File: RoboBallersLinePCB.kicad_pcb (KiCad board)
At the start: 2 copper layers, 116 parts, among them J2 Conn_01x04, J3 Conn_02x05_Odd_Even, Q1 SUD08P06-155L, Q2 BSP89, U1 MCP3008, U2 MCP3008, U3 MCP3008, U4 NSL-32, U5 NSL-32, U7 Solenoid-Electric

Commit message: gg
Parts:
- moved R7 97.8 mm to (35.8, 105.7)
- moved D1 83.9 mm to (84.2, 34.1)
- moved D2 83.9 mm to (84.2, 37.5)
- moved D3 83.9 mm to (84.2, 40.8)
- moved D37 83.9 mm to (88.2, 85.7)
- moved D38 83.9 mm to (88.2, 88.7)
- moved D39 83.9 mm to (88.2, 91.8)
- moved D4 83.9 mm to (84.2, 44.2)
- moved D40 83.9 mm to (88.2, 94.8)
- moved D41 83.9 mm to (88.2, 97.9)
- moved D42 83.9 mm to (88.2, 100.9)
- moved D5 83.9 mm to (84.2, 47.6)
- moved D6 83.9 mm to (84.2, 51.0)
- moved J2 83.9 mm to (107.5, 43.0)
- moved Q2 83.9 mm to (110.1, 36.6)
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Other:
- board outline added: 132 x 132 mm

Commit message: PCB + Footprint Revisions
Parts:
- removed J3: Conn_02x05_Odd_Even, Connector_PinHeader_2.54mm:PinHeader_2x05_P2.54mm_Vertical
- added J1: Conn_01x04, Connector_PinHeader_2.54mm:PinHeader_1x04_P2.54mm_Vertical, F.Cu at (331.5, 213.4)
- added U6: NSL-32, Package_DIP:DIP-4_W7.62mm, F.Cu at (326.6, 158.8)
- C1: value 80V 2200uf -> 80v 2200uf
- D1, D10, D11, D12, D13, D14, D15, D16, D17, D18, D19, D2, D20, D21, D22, D23, D24, D3, D4, D5, D6, D7, D8, D9: footprint LED_SMD:LED_1206_3216Metric_Pad1.42x1.75mm_HandSolder -> Capacitor_SMD:C_0805_2012Metric_Pad1.18x1.45mm_HandSolder; moved to B.Cu
- D25, D26, D27, D28, D29, D30, D31, D32, D33, D34, D35, D36, D37, D38, D39, D40, D41, D42, D43, D44, D45, D46, D47, D48: footprint LED_SMD:LED_0805_2012Metric_Pad1.15x1.40mm_HandSolder -> Capacitor_SMD:C_0805_2012Metric_Pad1.18x1.45mm_HandSolder; moved to B.Cu
- D49: value D -> Diode
- J2: value Conn_01x04 -> Bottom PCB; footprint Connector_PinHeader_2.54mm:PinHeader_1x04_P2.54mm_Vertical -> Connector_IDC:IDC-Header_2x05_P2.54mm_Vertical
- Q1: value SUD08P06-155L -> P-Channel; footprint Package_TO_SOT_SMD:TO-252-2 -> Package_TO_SOT_THT:TO-220-3_Vertical
- Q2: value BSP89 -> N-Channel; footprint Package_TO_SOT_SMD:SOT-223-3_TabPin2 -> Package_TO_SOT_THT:TO-220-3_Vertical
- R1, R18: value 750 -> 10k; footprint Resistor_SMD:R_1206_3216Metric_Pad1.30x1.75mm_HandSolder -> Capacitor_SMD:C_0805_2012Metric_Pad1.18x1.45mm_HandSolder
- R10, R11, R12, R13, R14, R15, R16, R17, R19, R2, R20, R21, R22, R23, R24, R3, R4, R5, R6, R8, R9: footprint Resistor_SMD:R_1206_3216Metric_Pad1.30x1.75mm_HandSolder -> Capacitor_SMD:C_0805_2012Metric_Pad1.18x1.45mm_HandSolder; moved to B.Cu
- R25, R26: value 14k -> 750; footprint Resistor_SMD:R_1210_3225Metric_Pad1.30x2.65mm_HandSolder -> Capacitor_SMD:C_0805_2012Metric_Pad1.18x1.45mm_HandSolder; moved to B.Cu
- R27: value 14k -> 10k; footprint Resistor_SMD:R_1210_3225Metric_Pad1.30x2.65mm_HandSolder -> Capacitor_SMD:C_0805_2012Metric_Pad1.18x1.45mm_HandSolder
- R28, R29, R30, R31, R32, R33, R34, R35, R36, R37, R38, R39, R40, R41, R42, R43, R44, R45, R46, R47, R48: footprint Resistor_SMD:R_1210_3225Metric_Pad1.30x2.65mm_HandSolder -> Capacitor_SMD:C_0805_2012Metric_Pad1.18x1.45mm_HandSolder; moved to B.Cu
- R49, R50, R51: value 10K -> 14k; footprint Resistor_THT:R_Axial_DIN0204_L3.6mm_D1.6mm_P7.62mm_Horizontal -> Capacitor_SMD:C_0805_2012Metric_Pad1.18x1.45mm_HandSolder; moved to B.Cu
- R52: value 5K -> 5k; footprint Resistor_SMD:R_0805_2012Metric_Pad1.20x1.40mm_HandSolder -> Capacitor_SMD:C_0805_2012Metric_Pad1.18x1.45mm_HandSolder
- R53: value 19K -> 19k; footprint Resistor_SMD:R_1206_3216Metric_Pad1.30x1.75mm_HandSolder -> Capacitor_SMD:C_0805_2012Metric_Pad1.18x1.45mm_HandSolder
- R54, R55: footprint Resistor_SMD:R_1206_3216Metric_Pad1.30x1.75mm_HandSolder -> Capacitor_SMD:C_0805_2012Metric_Pad1.18x1.45mm_HandSolder
- R56: value 10K -> 10k; footprint Resistor_THT:R_Axial_DIN0204_L3.6mm_D1.6mm_P7.62mm_Horizontal -> Capacitor_SMD:C_0805_2012Metric_Pad1.18x1.45mm_HandSolder
- R7: value 750 -> 165; footprint Resistor_SMD:R_1206_3216Metric_Pad1.30x1.75mm_HandSolder -> Capacitor_SMD:C_0805_2012Metric_Pad1.18x1.45mm_HandSolder; moved to B.Cu
- U1, U2, U3: footprint digikey-footprints:DIP-16_W7.62mm -> Package_DIP:DIP-16_W7.62mm_Socket
- U4: value NSL-32 -> BoostConverter; footprint OptoDevice:Luna_NSL-32 -> BoostConverter:Boost_Convertor_LM2577
- U5: footprint OptoDevice:Luna_NSL-32 -> Package_DIP:DIP-4_W7.62mm
- U7: footprint Connector_PinSocket_2.54mm:PinSocket_1x02_P2.54mm_Vertical -> KickerPad:KickerPad
- moved J2 284.7 mm to (345.4, 199.4)
- moved U7 268.7 mm to (348.8, 170.2)
- moved R1 253.8 mm to (280.2, 193.8)
- moved R18 247.1 mm to (285.0, 202.8)
- moved R53 246.3 mm to (299.4, 181.7)
- moved R54 246.2 mm to (299.4, 184.7)
- moved R55 246.1 mm to (299.4, 187.7)
- moved R27 243.7 mm to (289.8, 187.7)
- moved Q2 240.7 mm to (316.7, 159.9)
- moved U5 235.6 mm to (326.6, 152.1)
- moved C1 230.6 mm to (310.9, 209.5)
- moved R56 230.6 mm to (299.4, 190.7)
- moved D49 229.8 mm to (265.7, 219.7)
- moved R52 227.6 mm to (299.4, 178.7)
- moved Q1 223.1 mm to (316.7, 154.0)
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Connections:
- D25 pad 1: Net-(D25-K) -> CH01
- D26 pad 1: Net-(D26-K) -> CH11
- D27 pad 1: Net-(D27-K) -> CH21
- D28 pad 1: Net-(D28-K) -> CH31
- D29 pad 1: Net-(D29-K) -> CH41
- D30 pad 1: Net-(D30-K) -> CH51
- D31 pad 1: Net-(D31-K) -> CH61
- D32 pad 1: Net-(D32-K) -> CH71
- D33 pad 1: Net-(D33-K) -> CH02
- D34 pad 1: Net-(D34-K) -> CH12
- D35 pad 1: Net-(D35-K) -> CH22
- D36 pad 1: Net-(D36-K) -> CH32
- D37 pad 1: Net-(D37-K) -> CH42
- D38 pad 1: Net-(D38-K) -> CH52
- D39 pad 1: Net-(D39-K) -> CH62
- D40 pad 1: Net-(D40-K) -> CH72
- D41 pad 1: Net-(D41-K) -> CH03
- D42 pad 1: Net-(D42-K) -> CH13
- D43 pad 1: Net-(D43-K) -> CH23
- D44 pad 1: Net-(D44-K) -> CH33
- D45 pad 1: Net-(D45-K) -> CH43
- D46 pad 1: Net-(D46-K) -> CH53
- D47 pad 1: Net-(D47-K) -> CH63
- D48 pad 1: Net-(D48-K) -> CH73
- D49 pad 1: Net-(D49-K) -> Net-(D49-A)
- D49 pad 2: Net-(D49-A) -> Net-(D49-K)
- J2 pad 1: Kicker -> 12v
- J2 pad 2: 3.3V -> CSLS1
- J2 pad 3: GND -> 3.3v
- J2 pad 4: 12V -> CSLS2
- Q1 pad 2: Net-(D49-A) -> Net-(D49-K)
- Q1 pad 3: GND -> 48v
- Q2 pad 2: Net-(D49-K) -> Net-(D49-A)
- Q2 pad 3: 48v -> GND
- R1 pad 1: Net-(D1-A) -> CSLS1
- R1 pad 2: 3.3v -> unconnected-(R1-Pad2)
- R10 pad 1: Net-(D10-A) -> Net-(D9-A)
- R11 pad 1: Net-(D11-A) -> Net-(D10-A)
- R12 pad 1: Net-(D12-A) -> Net-(D11-A)
- R13 pad 1: Net-(D13-A) -> Net-(D12-A)
- R14 pad 1: Net-(D14-A) -> Net-(D13-A)
- R15 pad 1: Net-(D15-A) -> Net-(D14-A)
- R16 pad 1: Net-(D16-A) -> Net-(D15-A)
- R17 pad 1: Net-(D17-A) -> Net-(D16-A)
- R18 pad 1: Net-(D18-A) -> CSLS2
- R18 pad 2: 3.3v -> unconnected-(R18-Pad2)
- R19 pad 1: Net-(D19-A) -> Net-(D17-A)
- R2 pad 1: Net-(D2-A) -> Net-(D1-A)
- R20 pad 1: Net-(D20-A) -> Net-(D18-A)
- R21 pad 1: Net-(D21-A) -> Net-(D19-A)
- R22 pad 1: Net-(D22-A) -> Net-(D20-A)
- R23 pad 1: Net-(D23-A) -> Net-(D21-A)
- R24 pad 1: Net-(D24-A) -> Net-(D22-A)
- R25 pad 1: GND -> Net-(D23-A)
- R25 pad 2: Net-(D26-K) -> 3.3v
- R26 pad 1: GND -> Net-(D24-A)
- R26 pad 2: Net-(D25-K) -> 3.3v
- R27 pad 1: GND -> CSLS3
- R27 pad 2: Net-(D27-K) -> unconnected-(R27-Pad2)
- R28 pad 1: GND -> CH01
- R28 pad 2: Net-(D28-K) -> GND
- R29 pad 1: GND -> CH11
- R29 pad 2: Net-(D29-K) -> GND
- R3 pad 1: Net-(D3-A) -> Net-(D2-A)
- R30 pad 1: GND -> CH21
- R30 pad 2: Net-(D30-K) -> GND
- R31 pad 1: GND -> CH31
- R31 pad 2: Net-(D31-K) -> GND
- R32 pad 1: GND -> CH41
- R32 pad 2: Net-(D32-K) -> GND
- R33 pad 1: GND -> CH51
- R33 pad 2: Net-(D33-K) -> GND
- R34 pad 1: GND -> CH61
- R34 pad 2: Net-(D34-K) -> GND
- R35 pad 1: GND -> CH71
- R35 pad 2: Net-(D35-K) -> GND
- R36 pad 1: GND -> CH02
- R36 pad 2: Net-(D36-K) -> GND
- R37 pad 1: GND -> CH12
- R37 pad 2: Net-(D37-K) -> GND
- R38 pad 1: GND -> CH22
- R38 pad 2: Net-(D38-K) -> GND
- R39 pad 1: GND -> CH32
- R39 pad 2: Net-(D39-K) -> GND
- R4 pad 1: Net-(D4-A) -> Net-(D3-A)
- R40 pad 1: GND -> CH42
- R40 pad 2: Net-(D40-K) -> GND
- R41 pad 1: GND -> CH52
- R41 pad 2: Net-(D41-K) -> GND
- R42 pad 1: GND -> CH62
- R42 pad 2: Net-(D42-K) -> GND
- R43 pad 1: GND -> CH72
- R43 pad 2: Net-(D43-K) -> GND
- R44 pad 1: GND -> CH03
- R44 pad 2: Net-(D44-K) -> GND
- R45 pad 1: GND -> CH13
- R45 pad 2: Net-(D45-K) -> GND
- R46 pad 1: GND -> CH23
- R46 pad 2: Net-(D46-K) -> GND
- R47 pad 1: GND -> CH33
- R47 pad 2: Net-(D47-K) -> GND
- R48 pad 1: GND -> CH43
- R48 pad 2: Net-(D48-K) -> GND
- R49 pad 1: CSLS1 -> CH53
- R49 pad 2: 3.3V -> GND
- R5 pad 1: Net-(D5-A) -> Net-(D4-A)
- R50 pad 1: CSLS2 -> CH63
- R50 pad 2: 3.3V -> GND
- R51 pad 1: CSLS2 -> CH73
- R51 pad 2: 3.3V -> GND
- R52 pad 1: 48V -> 48v
- R52 pad 2: Net-(Q2-G) -> Net-(Q1-G)
- R53 pad 1: Net-(Q2-G) -> Net-(Q1-G)
- R54 pad 2: Net-(U4-A) -> Net-(U5-A)
- R55 pad 2: Net-(U5-A) -> Net-(U6-A)
- R56 pad 1: Net-(Q1-G) -> Net-(Q2-G)
- R6 pad 1: Net-(D6-A) -> Net-(D5-A)
- R7 pad 1: Net-(D7-A) -> Net-(D6-A)
- R8 pad 1: Net-(D8-A) -> Net-(D7-A)
- R9 pad 1: Net-(D9-A) -> Net-(D8-A)
- U1 pad 1: LS1 -> CH01
- U1 pad 15: 3.3V -> 3.3v
- U1 pad 16: 3.3V -> 3.3v
- U1 pad 2: LS2 -> CH11
- U1 pad 3: LS3 -> CH21
- U1 pad 4: LS4 -> CH31
- U1 pad 5: LS5 -> CH41
- U1 pad 6: LS6 -> CH51
- U1 pad 7: LS7 -> CH61
- U1 pad 8: LS8 -> CH71
- U2 pad 1: LS9 -> CH02
- U2 pad 15: 3.3V -> 3.3v
- U2 pad 16: 3.3V -> 3.3v
- U2 pad 2: LS10 -> CH12
- U2 pad 3: LS11 -> CH22
- U2 pad 4: LS12 -> CH32
- U2 pad 5: LS13 -> CH42
- U2 pad 6: LS14 -> CH52
- U2 pad 7: LS15 -> CH62
- U2 pad 8: LS16 -> CH72
- U3 pad 1: LS17 -> CH03
- U3 pad 10: CSLS2 -> CSLS3
- U3 pad 15: 3.3V -> 3.3v
- U3 pad 16: 3.3V -> 3.3v
- U3 pad 2: LS18 -> CH13
- U3 pad 3: LS19 -> CH23
- U3 pad 4: LS20 -> CH33
- U3 pad 5: LS21 -> CH43
- U3 pad 6: LS22 -> CH53
- U3 pad 7: LS23 -> CH63
- U3 pad 8: LS24 -> CH73
- U4 pad 1: Net-(U4-A) -> 12v
- U4 pad 3: Net-(Q2-G) -> 48v
- U4 pad 4: 48V -> GND
- U5 pad 4: 12V -> 48v
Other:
- board size 132 x 132 mm -> 1986.9 x 1987 mm

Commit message: More PCB Stuff
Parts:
- U3: moved to B.Cu
- moved U7 266.0 mm to (91.4, 102.9)
- moved J2 256.3 mm to (108.0, 103.0), turned to 90 degrees
- moved C1 169.3 mm to (234.5, 58.4)
- moved Q1 142.6 mm to (177.8, 121.6)
- moved U4 138.4 mm to (93.3, 73.0), turned to 90 degrees
- moved J1 126.7 mm to (205.7, 198.1)
- moved R1 126.7 mm to (154.4, 178.5)
- moved R18 126.7 mm to (159.2, 187.5)
- moved R27 126.7 mm to (164.1, 172.5)
- moved R52 126.7 mm to (173.7, 163.5)
- moved R53 126.7 mm to (173.7, 166.5)
- moved R54 126.7 mm to (173.7, 169.5)
- moved R55 126.7 mm to (173.7, 172.5)
- moved R56 126.7 mm to (173.7, 175.5)
- moved D49 126.7 mm to (140.0, 204.5)
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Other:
- outline, holes or cut-outs redrawn

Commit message: Idk
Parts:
- moved D1 370.8 mm to (356.0, 300.0), turned to 0 degrees
- moved R51 370.6 mm to (355.9, 296.3), turned to 3.75 degrees
- moved R2 370.6 mm to (355.9, 303.7), turned to -3.75 degrees
- moved D48 370.0 mm to (355.5, 292.7), turned to 7.5 degrees
- moved D25 370.0 mm to (355.5, 307.3), turned to -7.5 degrees
- moved R26 369.0 mm to (354.9, 289.1), turned to 11.25 degrees
- moved R28 369.0 mm to (354.9, 310.9), turned to -11.25 degrees
- moved D24 367.7 mm to (354.1, 285.5), turned to 15 degrees
- moved D2 367.6 mm to (354.1, 314.5), turned to -15 degrees
- moved R50 365.9 mm to (353.0, 282.0), turned to 18.75 degrees
- moved R3 365.8 mm to (353.0, 318.0), turned to -18.75 degrees
- moved U1 364.2 mm to (320.7, 348.6), turned to 180 degrees
- moved D47 363.7 mm to (351.7, 278.6), turned to 22.5 degrees
- moved D26 363.6 mm to (351.7, 321.4), turned to -22.5 degrees
- moved R25 361.2 mm to (350.2, 275.2), turned to 26.25 degrees
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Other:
- board size 1986.9 x 1987 mm -> 2187 x 2187 mm

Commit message: good stuff
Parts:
- moved J2 11.6 mm to (284.0, 330.2), turned to 0 degrees
- turned D26 to -22 degrees
- turned D29 to -67 degrees
- turned D32 to -112 degrees
- turned D47 to 23 degrees
- turned D35 to -157 degrees
- turned D44 to 68 degrees
- turned D38 to 158 degrees
- turned D41 to 113 degrees
- turned R28 to -11 degrees
- turned R7 to -79 degrees
- turned R13 to -169 degrees
- turned R46 to 79 degrees
- turned R26 to 11 degrees
- turned R34 to -101 degrees
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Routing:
- net GND: track 0.00 -> 659.4 mm, vias 0 -> 5
- net 3.3v: track 0.00 -> 449.7 mm, vias 0 -> 4
- net SCK1: track 0.00 -> 163.4 mm, vias 0 -> 4
- net MISO: track 0.00 -> 153.8 mm, vias 0 -> 3
- net MOSI: track 0.00 -> 150.0 mm, vias 0 -> 4
- net 12v: track 0.00 -> 145.5 mm
- net Net-(D49-K): track 0.00 -> 110.3 mm, vias 0 -> 3
- net Kicker: track 0.00 -> 105.9 mm, vias 0 -> 1
- net CH13: track 0.00 -> 105.0 mm, vias 0 -> 4
- net CH23: track 0.00 -> 101.8 mm, vias 0 -> 2
- net Net-(Q2-G): track 0.00 -> 97.3 mm, vias 0 -> 1
- net CSLS3: track 0.00 -> 84.7 mm
- net CH33: track 0.00 -> 81.4 mm, vias 0 -> 4
- net CH43: track 0.00 -> 78.8 mm
- net 48v: track 0.00 -> 77.8 mm
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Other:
- board size 2187 x 2187 mm -> 132 x 132 mm

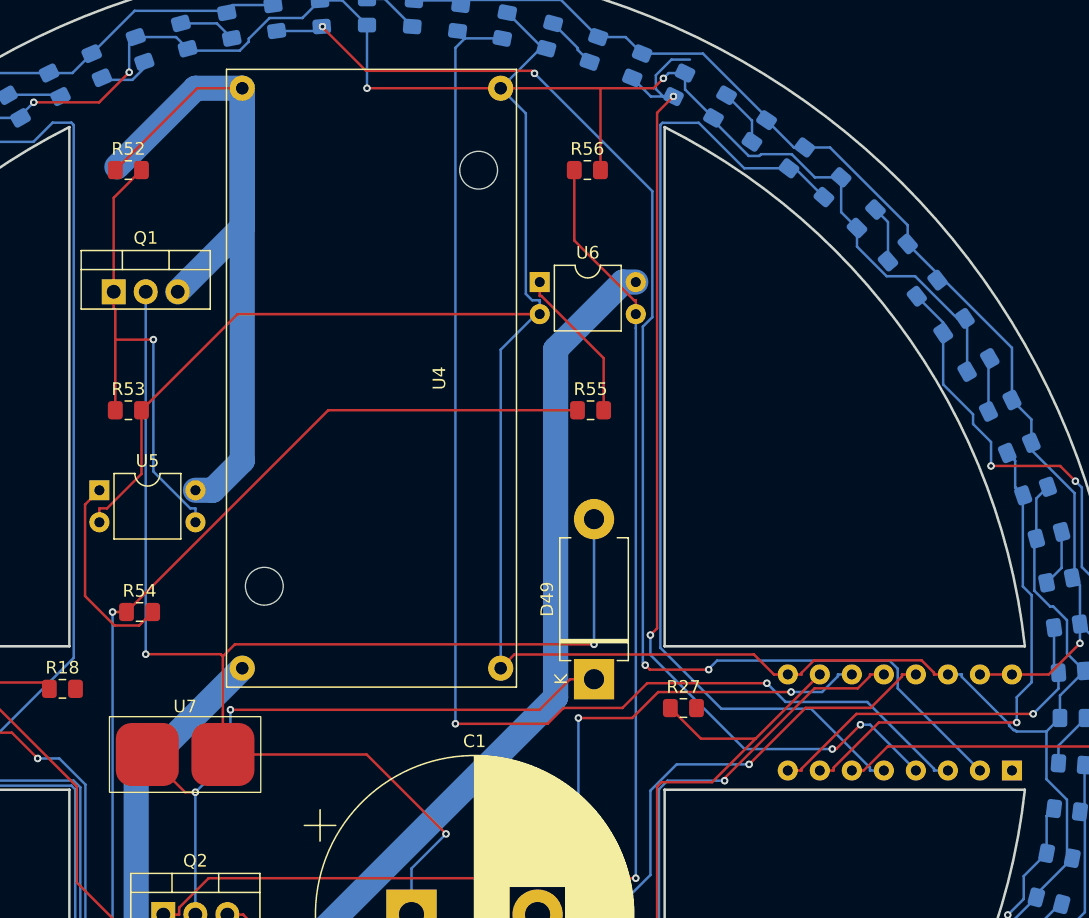
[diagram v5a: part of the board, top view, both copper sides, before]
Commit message: Added Vias, board done
 - Need to fix outline errors
 - Need to look at other errors, are they important?
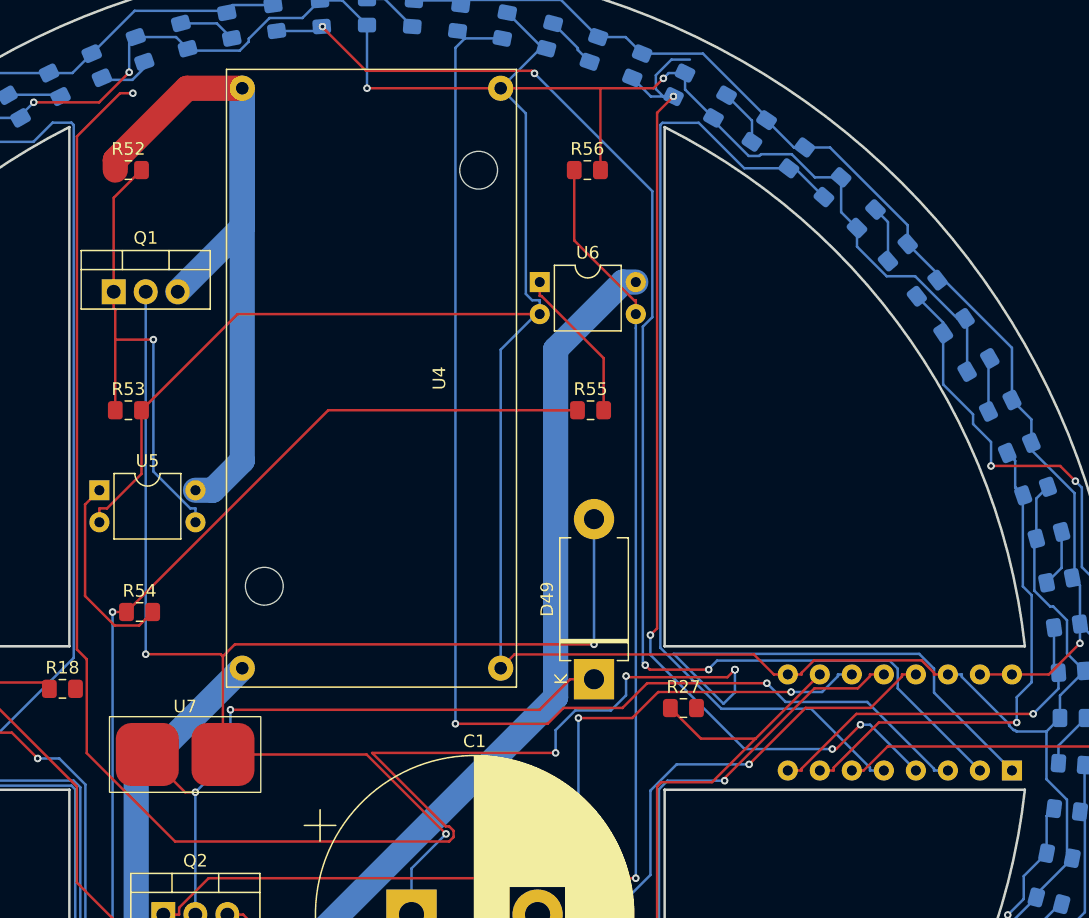
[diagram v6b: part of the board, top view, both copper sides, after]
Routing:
- net CH03: track 4.31 -> 175.1 mm, vias 0 -> 5
- net 48v: track 77.8 -> 65.7 mm

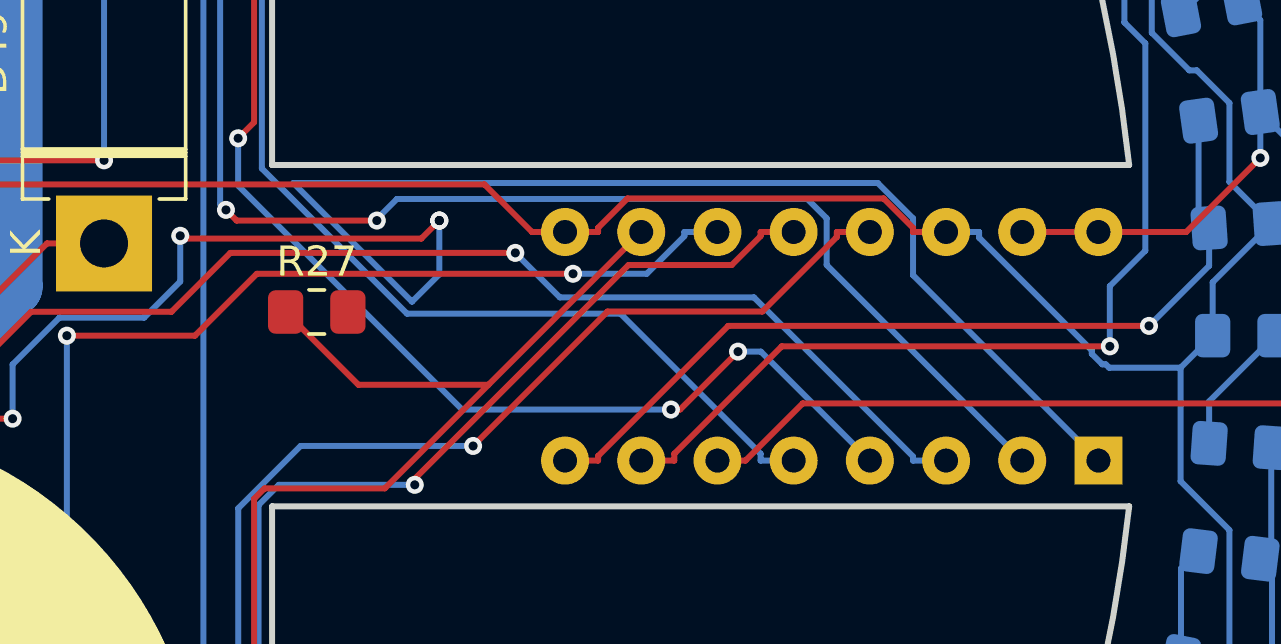
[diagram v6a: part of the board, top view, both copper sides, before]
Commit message: Changed One Via
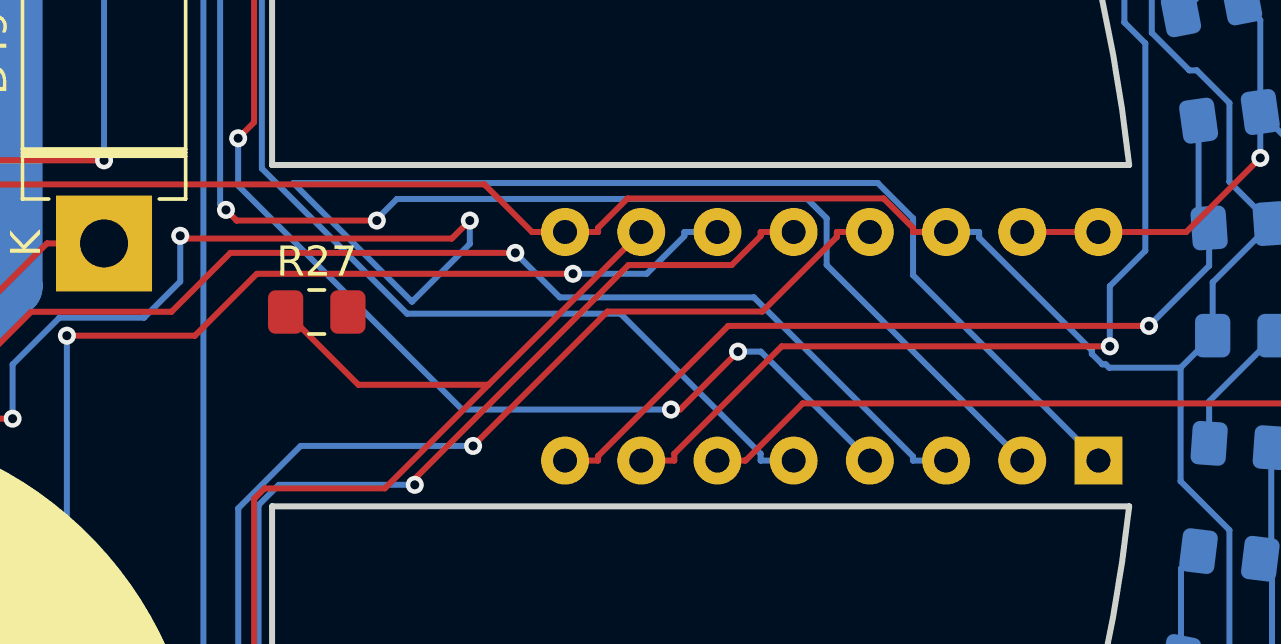
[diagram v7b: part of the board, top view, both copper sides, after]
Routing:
- net CH03: track 175.1 -> 176.5 mm, vias 5 -> 4
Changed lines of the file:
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@@
+	)
+	(segment
+		(start 330.2 296.164)
+		(end 329.6 296.764)
+		(width 0.2)
+		(layer "F.Cu")
+		(net 55)
+	)
+	(segment
+		(start 320.64 296.764)
+		(end 320.548 296.672)
+		(width 0.2)
+		(layer "F.Cu")
+		(net 55)
 	)
 	(segment
@@
 	)
 	(segment
-		(start 329.184 296.164)
-		(end 328.584 296.764)
-		(width 0.2)
-		(layer "F.Cu")
-		(net 55)
-	)
-	(segment
 		(start 276.990333 294.560681)
 		(end 276.990333 253.869667)
@@
 	)
 	(segment
-		(start 320.64 296.764)
-		(end 320.548 296.672)
-		(width 0.2)
-		(layer "F.Cu")
-		(net 55)
-	)
-	(segment
 		(start 314.96 302.768)
 		(end 300.406286 302.768)
@@
 	)
 	(segment
-		(start 328.584 296.764)
+		(start 329.6 296.764)
 		(end 320.64 296.764)
 		(width 0.2)
@@
 	)
 	(via
-		(at 329.184 296.164)
-		(size 0.6)
-		(drill 0.3)
-		(layers "F.Cu" "B.Cu")
-		(net 55)
-	)
-	(via
-		(at 329.184 296.164)
-		(size 0.6)
-		(drill 0.3)
-		(layers "F.Cu" "B.Cu")
+		(at 330.2 296.164)
+		(size 0.6)
+		(drill 0.3)
+		(layers "F.Cu" "B.Cu")
+		(net 55)
+	)
+	(segment
+		(start 328.273786 298.8682)
+		(end 324.317739 294.912153)
+		(width 0.2)
+		(layer "B.Cu")
 		(net 55)
 	)
@@
 	)
 	(segment
+		(start 330.2 296.164)
+		(end 330.2 296.941986)
+		(width 0.2)
+		(layer "B.Cu")
+		(net 55)
+	)
+	(segment
 		(start 278.9667 249.2212)
 		(end 279.1311 249.3856)
@@
 	)
 	(segment
+		(start 324.317739 294.912153)
+		(end 343.797788 294.912153)
+		(width 0.2)
+		(layer "B.Cu")
+		(net 55)
+	)
+	(segment
+		(start 330.2 296.941986)
+		(end 328.273786 298.8682)
+		(width 0.2)
+		(layer "B.Cu")
+		(net 55)
+	)
+	(segment
 		(start 316.520671 299.4012)
 		(end 314.96 300.961871)
@@
 	)
 	(segment
-		(start 344.975 297.985)
-		(end 344.975 296.089365)
-		(width 0.2)
-		(layer "B.Cu")
-		(net 55)
-	)
-	(segment
 		(start 282.3329 248.4386)
 		(end 282.3329 247.9543)
@@
 	)
 	(segment
+		(start 344.975 296.089365)
+		(end 344.975 297.985)
+		(width 0.2)
+		(layer "B.Cu")
+		(net 55)
+	)
+	(segment
+		(start 343.797788 294.912153)
+		(end 344.975 296.089365)
+		(width 0.2)
+		(layer "B.Cu")
+		(net 55)
+	)
+	(segment
 		(start 279.1311 249.3856)
 		(end 281.3859 249.3856)
@@
 	)
 	(segment
-		(start 328.273786 298.8682)
-		(end 329.184 297.957986)
-		(width 0.2)
-		(layer "B.Cu")
-		(net 55)
-	)
-	(segment
-		(start 343.797788 294.912153)
-		(end 324.317739 294.912153)
-		(width 0.2)
-		(layer "B.Cu")
-		(net 55)
-	)
-	(segment
-		(start 351.155 304.165)
-		(end 344.975 297.985)
+		(start 344.975 297.985)
+		(end 351.155 304.165)
 		(width 0.2)
 		(layer "B.Cu")
@@
 		(width 0.2)
 		(layer "B.Cu")
-		(net 55)
-	)
-	(segment
-		(start 344.975 296.089365)
-		(end 343.797788 294.912153)
-		(width 0.2)
-		(layer "B.Cu")
-		(net 55)
-	)
-	(segment
-		(start 324.317739 294.912153)
-		(end 328.273786 298.8682)
-		(width 0.2)
-		(layer "B.Cu")
-		(net 55)
-	)
-	(segment
-		(start 329.184 297.957986)
-		(end 329.184 296.164)
-		(width 0.2)
-		(layer "B.Cu")
